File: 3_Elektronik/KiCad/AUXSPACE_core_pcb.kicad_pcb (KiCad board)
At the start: 4 copper layers, 60 x 60 mm, 86 parts, among them J1 Conn_02x10_Odd_Even, J2 Conn_02x10_Odd_Even, J3 Conn_02x10_Odd_Even, J4 Conn_02x10_Odd_Even, J5 Conn_01x04_Pin, J6 693072010801, J7 629722000214, Q1 2N7002K, Q2 2N7002K, SW2 434331013822, SW3 434331013822, U1 LSM6DSV320XTR, U2 TPS7B8601QDDARQ1, U3 TCAN334, U4 ESP32-S3-WROOM-1, U5 LSM6DSO32XTR, U6 DPS310, U7 LIS3MDL, U8 CH224A

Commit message: fix: :bug: USB PD being 5V
USB PD is now set to 9V via I/O level configuration
as described in chapter 5.2.2 and table 5-2 in the
CH224A datasheet:

| CFG1 | CFG2 | CFG3 | Voltage |
|:----:|:----:|:---:-|--------:|
| 0    | 0    | 0    |  9V     |
| 0    | 0    | 1    | 12V     |
| 0    | 1    | 1    | 20V     |
| 0    | 1    | 0    | 28V     |
| 1    | X    | X    |  5V     |
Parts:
- removed R31: 6,8k, Resistor_SMD:R_0603_1608Metric
- moved R23 0.06 mm to (123.5, 84.0)
- moved R34 0.06 mm to (125.1, 84.0), turned to 90 degrees
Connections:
- R34 pad 1: Net-(Q2-G) -> Net-(U8-PG)
- R34 pad 2: Net-(U8-PG) -> Net-(Q2-G)
- U5 pad 12: unconnected-(U5-CS-Pad12) -> +3V3
- U8 pad 2: unconnected-(U8-CFG2/SCL-Pad2) -> GND
- U8 pad 3: unconnected-(U8-CFG3/SDA-Pad3) -> GND
- U8 pad 9: Net-(U8-CFG1) -> GND
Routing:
- net GND: track 242.6 -> 249.1 mm
- net Net-(U8-CFG1): track 2.20 -> 0.00 mm
- net +3V3: track 80.3 -> 81.8 mm, vias 12 -> 13

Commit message: style: :art: cleanup pcb
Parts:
- R23: value 390R -> 4,7k
- moved C13 2.42 mm to (168.3, 110.9), turned to 180 degrees
- moved R15 2.36 mm to (169.0, 113.2), turned to 90 degrees
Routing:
- net /Baseboard/I2C0_SCL: track 30.2 -> 27.3 mm
- net GND: track 249.1 -> 246.8 mm
- net +3V3: track 81.8 -> 83.7 mm
- net VBus_direct: track 58.9 -> 60.6 mm

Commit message: fix: :bug: keep out zone overlap
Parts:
- moved J5 0.40 mm to (171.6, 87.0)
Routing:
- net /Baseboard/LIFTOFF: track 54.2 -> 43.3 mm, vias 1 -> 2
- net /Baseboard/Power Fault: track 61.6 -> 51.9 mm, vias 1 -> 2
- net /Baseboard/UART_RX_bot: track 51.2 -> 53.0 mm, vias 2 -> 0
- net /Baseboard/ARM: track 26.8 -> 28.3 mm

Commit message: chore: update after review
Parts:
- removed C11: 100nF, Capacitor_SMD:C_0603_1608Metric
- added C25: 10µF, Capacitor_SMD:C_0603_1608Metric, F.Cu at (151.5, 83.7)
- Q2: value 2N7002K -> DMP3099L
- R18, R21, R22: value 390R -> 2,7k
- moved C8 0.60 mm to (157.6, 105.9)
- moved C7 0.60 mm to (157.6, 104.4)
- moved R2 0.15 mm to (163.9, 117.3)
- moved R17 0.11 mm to (160.9, 117.2)
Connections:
- SW3 pad 1: /Baseboard/IO0 -> Net-(R23-Pad2)
- SW3 pad 2: /Baseboard/IO0 -> Net-(R23-Pad2)
- SW3 pad 3: Net-(R23-Pad2) -> /Baseboard/IO0
- SW3 pad 4: Net-(R23-Pad2) -> /Baseboard/IO0
- SW3 pad 5: Net-(R23-Pad2) -> /Baseboard/IO0
- SW3 pad 6: Net-(R23-Pad2) -> /Baseboard/IO0
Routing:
- net GND: track 247.0 -> 251.9 mm, vias 36 -> 37
- net /Baseboard/IO0: track 38.8 -> 42.6 mm, vias 1 -> 0
- net +3V3: track 83.7 -> 85.9 mm, vias 13 -> 12
- net Net-(Q2-G): track 14.0 -> 13.0 mm, vias 2 -> 0
- net /Baseboard/ARM: track 28.3 -> 27.7 mm

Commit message: style: :art: split schematics into subpages
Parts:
- D3, D4, D5: value grün -> green
- turned R34 to -90 degrees
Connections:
- net /Baseboard/ACCEL_INT1 renamed /MCU/ACCEL_INT1
- net /Baseboard/BARO_INT renamed /MCU/BARO_INT
- net /Baseboard/Buzzer renamed /MCU/Buzzer
- net /Baseboard/CAN_RXD renamed /MCU/CAN_RXD
- net /Baseboard/CAN_SHDN renamed /MCU/CAN_SHDN
- net /Baseboard/CAN_STB renamed /MCU/CAN_STB
- net /Baseboard/CAN_TXD renamed /MCU/CAN_TXD
- net /Baseboard/CC1 renamed /Power/CC1
- net /Baseboard/CC2 renamed /Power/CC2
- net /Baseboard/I2C0_SCL renamed /MCU/I2C0_SCL
- net /Baseboard/I2C0_SDA renamed /MCU/I2C0_SDA
- net /Baseboard/IMU_INT renamed /MCU/IMU_INT
- net /Baseboard/IO0 renamed /MCU/IO0
- net /Baseboard/MAG_DRDY renamed /MCU/MAG_DRDY
- net /Baseboard/RX renamed /MCU/RX
- net /Baseboard/SD_CD/DAT3_CS renamed /MCU/SD_CD/DAT3_CS
- net /Baseboard/SD_CLK renamed /MCU/SD_CLK
- net /Baseboard/SD_CMD_MOSI renamed /MCU/SD_CMD_MOSI
- net /Baseboard/SD_DAT0_MISO renamed /MCU/SD_DAT0_MISO
- net /Baseboard/SD_DAT1 renamed /MCU/SD_DAT1
- net /Baseboard/SD_DAT2 renamed /MCU/SD_DAT2
- net /Baseboard/SD_LED renamed /MCU/SD_LED
- net /Baseboard/STATE_LED renamed /MCU/STATE_LED
- net /Baseboard/TX renamed /MCU/TX
- net /Baseboard/USB_D+ renamed /Power/USB_D+
- net /Baseboard/USB_D- renamed /Power/USB_D-
- net Net-(U4-EN) renamed /MCU/MCU_EN
- R34 pad 1: Net-(U8-PG) -> Net-(Q2-G)
- R34 pad 2: Net-(Q2-G) -> Net-(U8-PG)

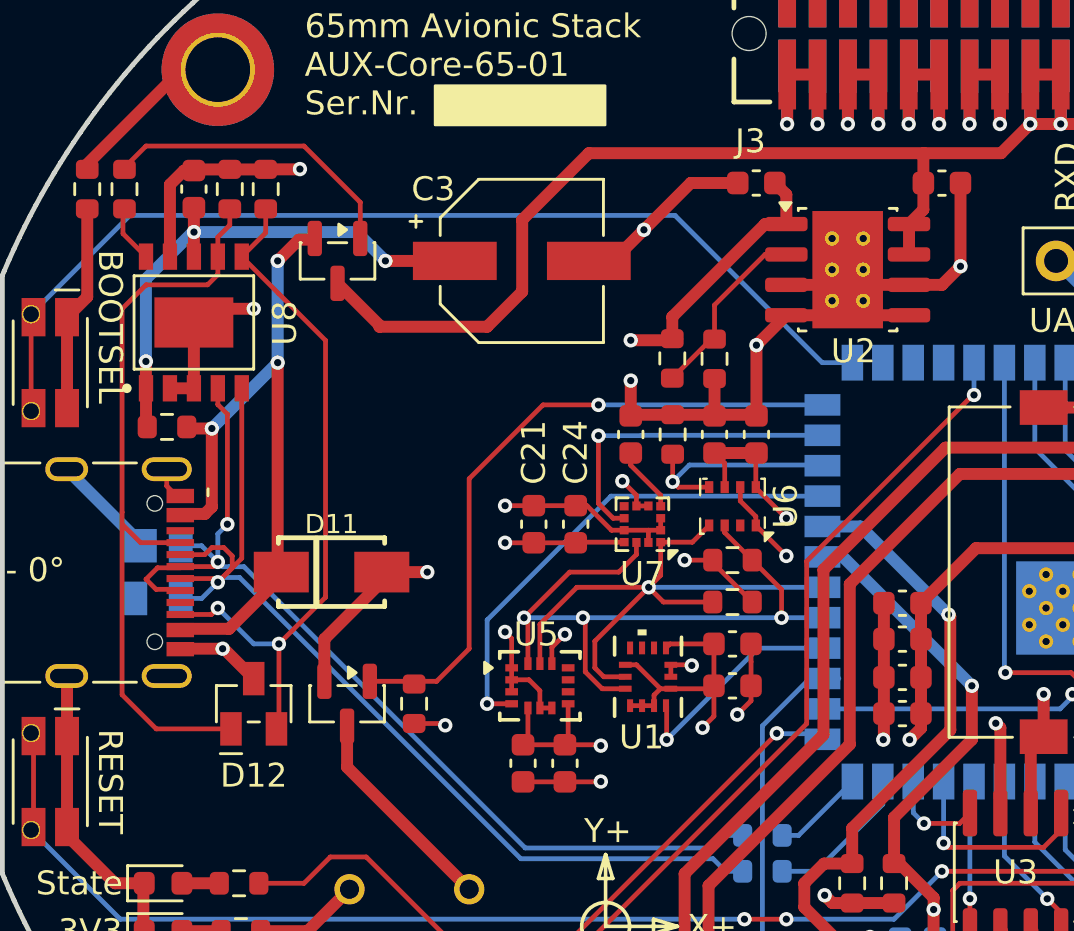
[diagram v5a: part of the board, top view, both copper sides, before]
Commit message: fix: move D11 in current path
This commit also fixes the messed-up footprint of J1
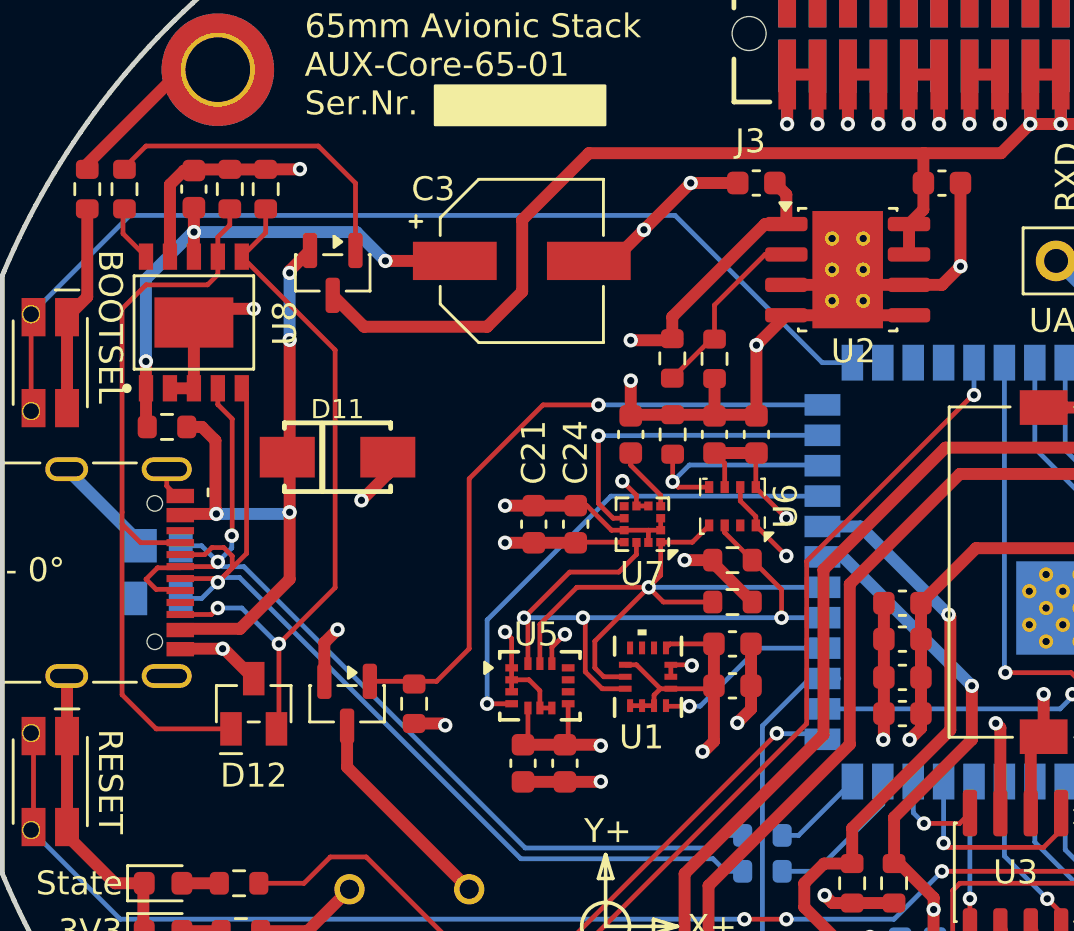
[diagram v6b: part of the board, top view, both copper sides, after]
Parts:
- moved D11 4.81 mm to (134.0, 95.2)
- moved Q2 0.54 mm to (133.8, 87.5)
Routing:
- net GND: track 251.9 -> 249.3 mm, vias 37 -> 39
- net /MCU/ACCEL_INT1: track 9.53 -> 7.56 mm
- net Vusb: track 30.9 -> 29.7 mm, vias 3 -> 4
- net +3V3: track 85.9 -> 87.0 mm
- net Net-(Q2-G): track 13.0 -> 13.6 mm
